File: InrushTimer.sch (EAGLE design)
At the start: 71 parts, among them IC1 TLC272D, IC2 555, IC3 4076N, Q2 TRANSISTOR-FET_2N7002, Q3 TRANSISTOR-FET_2N7002, Q4 TRANSISTOR-FET_2N7002, Q5 TRANSISTOR-FET_2N7002, Q6 DIODES_ZTX451DIODES_ZTX451_0_0, T1 MMBTA05, U1 ROHM_BY_ELEMENT14_BATCH_1_BU4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

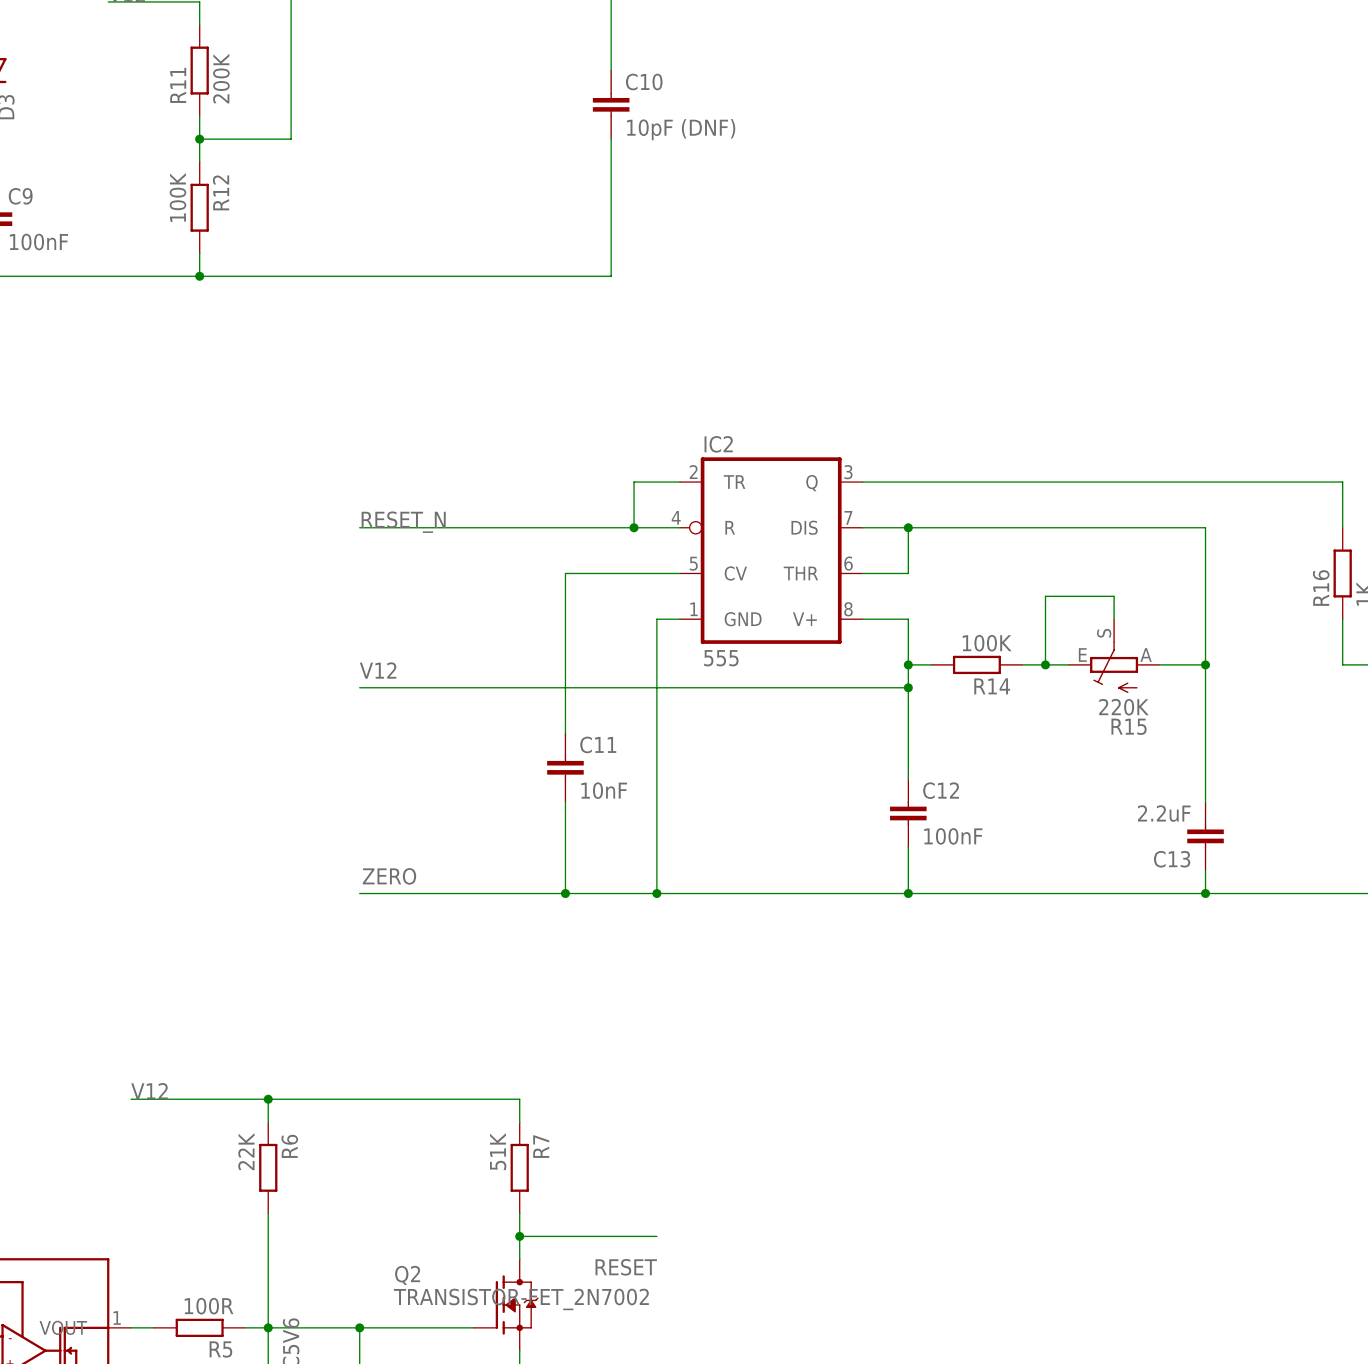
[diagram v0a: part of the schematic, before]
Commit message: Refitted the timer and pulse generator.
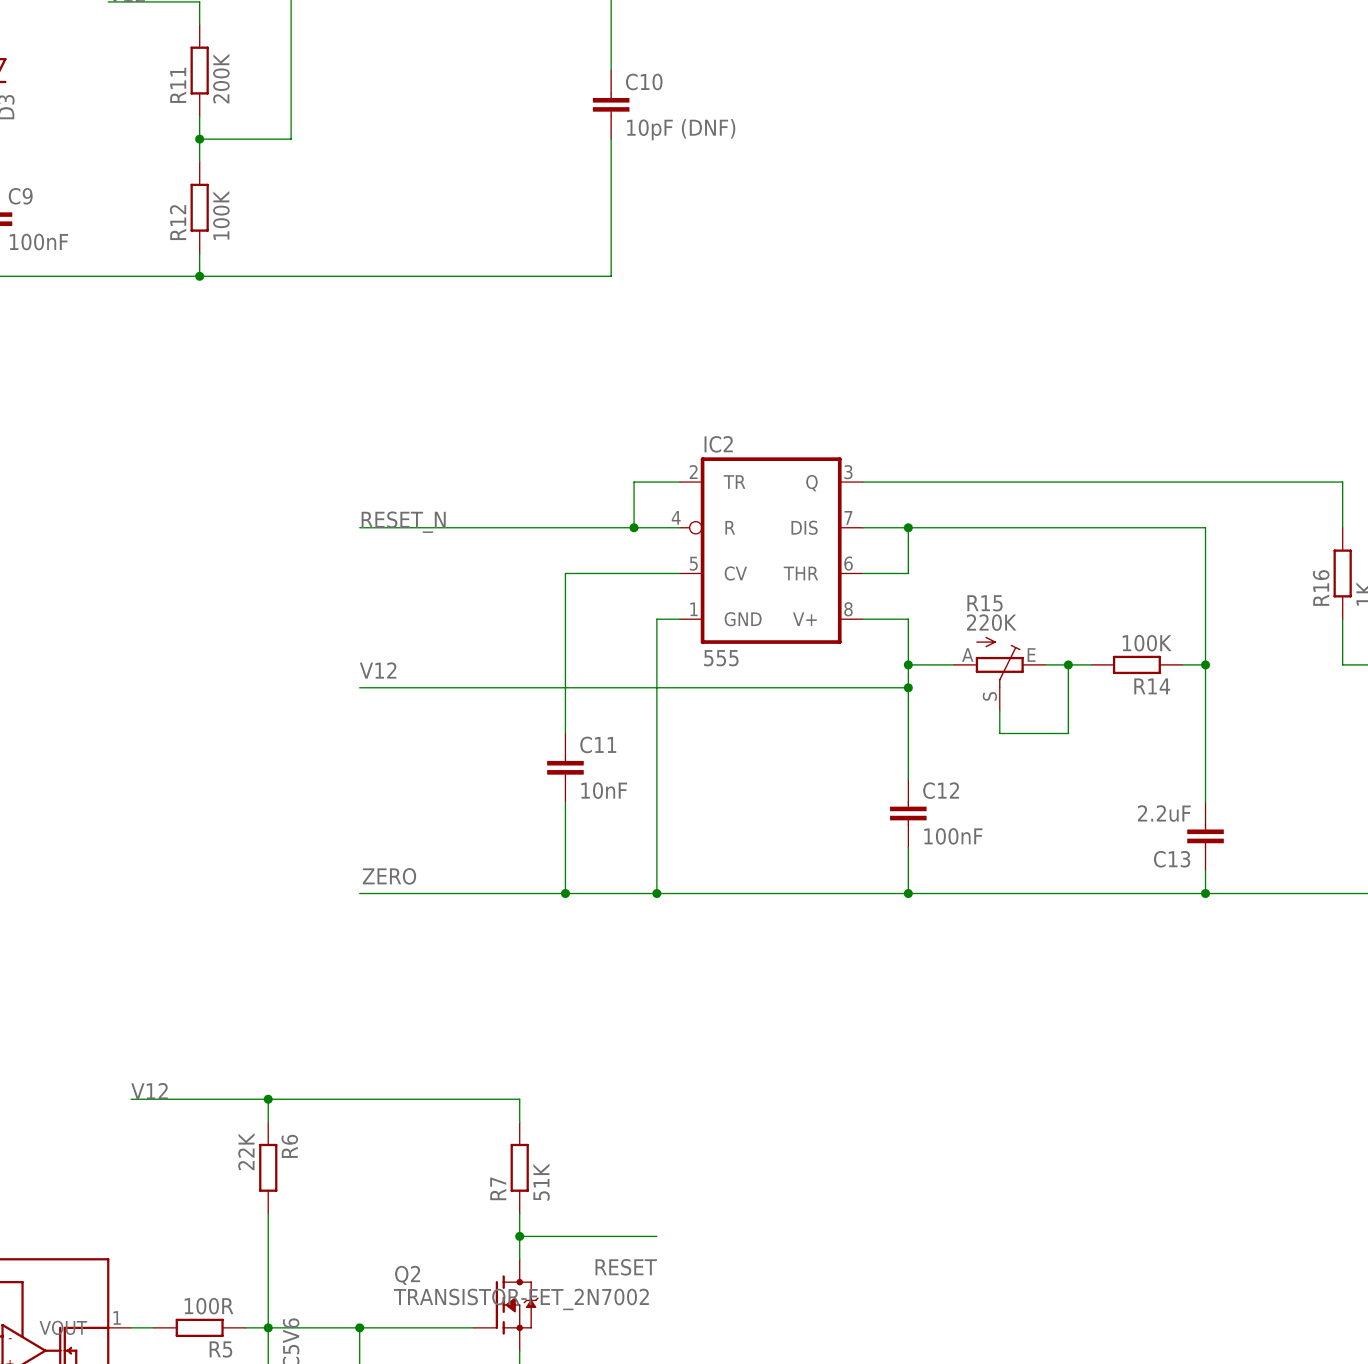
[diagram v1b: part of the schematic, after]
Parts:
- D5: device diode:DIODE-DP41-10V -> diode:DIODE-DO41-10VN
- D6: device diode:DIODE-DP41-10V -> diode:DIODE-DO41-7.6
- R15: device pot:TRIM_EU-CA6H_MOD -> pot:TRIM_EU-CA6H
- R7: device rcl:R-EU_0207/7 -> rcl:R-EU_0207/2V
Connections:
- net N$2: now also R14.2; no longer R14.1
- net N$28: now also R14.1; no longer R15.A
- net RESET: now also R7.1; no longer R7.2
- net THRESH: now also R12.2; no longer R12.1
- net V12: now also R15.A, R7.2; no longer R14.2, R7.1
- net ZERO: now also R12.1; no longer R12.2
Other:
- moved on the sheet: R12, R14, R15, R7
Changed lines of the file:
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@@
 <part name="R1" library="rcl" deviceset="R-EU_" device="0207/2V" value="4K7"/>
 <part name="R8" library="rcl" deviceset="R-EU_" device="0207/2V" value="22K"/>
-<part name="D5" library="diode" deviceset="DIODE-" device="DP41-10V" value="1n4001"/>
+<part name="D5" library="diode" deviceset="DIODE-" device="DO41-10VN" value="1n4001"/>
 <part name="R9" library="rcl" deviceset="R-EU_" device="0207/7" value="9.1M"/>
 <part name="R11" library="rcl" deviceset="R-EU_" device="0207/2V" value="200K"/>
 <part name="R12" library="rcl" deviceset="R-EU_" device="0207/2V" value="100K"/>
 <part name="IC3" library="40xx" deviceset="4076" device="N"/>
-<part name="D6" library="diode" deviceset="DIODE-" device="DP41-10V" value="1n4001"/>
+<part name="D6" library="diode" deviceset="DIODE-" device="DO41-7.6" value="1n4001"/>
 <part name="R13" library="rcl" deviceset="R-EU_" device="0207/2V" value="200K"/>
 <part name="R2" library="rcl" deviceset="R-EU_" device="0207/7" value="27K"/>
-<part name="R7" library="rcl" deviceset="R-EU_" device="0207/7" value="51K"/>
+<part name="R7" library="rcl" deviceset="R-EU_" device="0207/2V" value="51K"/>
 <part name="R6" library="rcl" deviceset="R-EU_" device="0207/2V" value="22K"/>
 <part name="R3" library="rcl" deviceset="R-EU_" device="0207/2V" value="10K"/>
@@
 <part name="R17" library="rcl" deviceset="R-EU_" device="0207/2V" value="51K"/>
 <part name="C12" library="rcl" deviceset="C-EU" device="050-024X044" value="100nF"/>
-<part name="R15" library="pot" deviceset="TRIM_EU-" device="CA6H_MOD" value="220K"/>
+<part name="R15" library="pot" deviceset="TRIM_EU-" device="CA6H" value="220K"/>
 <part name="X4" library="con-wago-500" deviceset="W237-102" device=""/>
 <part name="C11" library="rcl" deviceset="C-EU" device="050-024X044" value="10nF"/>
@@
 <instance part="R9" gate="G$1" x="-38.1" y="45.72" rot="R90"/>
 <instance part="R11" gate="G$1" x="0" y="60.96" rot="R90"/>
-<instance part="R12" gate="G$1" x="0" y="45.72" rot="R270"/>
+<instance part="R12" gate="G$1" x="0" y="45.72" rot="R90"/>
 <instance part="IC3" gate="A" x="223.52" y="-7.62"/>
 <instance part="IC3" gate="P" x="190.5" y="-20.32"/>
@@
 <instance part="R13" gate="G$1" x="22.86" y="91.44" rot="R180"/>
 <instance part="R2" gate="G$1" x="-73.66" y="-55.88" rot="R90"/>
-<instance part="R7" gate="G$1" x="35.56" y="-60.96" rot="R270"/>
+<instance part="R7" gate="G$1" x="35.56" y="-60.96" rot="R90"/>
 <instance part="R6" gate="G$1" x="7.62" y="-60.96" rot="R270"/>
 <instance part="R3" gate="G$1" x="-73.66" y="-76.2" rot="R90"/>
@@
 <instance part="C6" gate="G$1" x="-35.56" y="68.58" rot="R90"/>
 <instance part="C8" gate="G$1" x="-27.94" y="101.6"/>
-<instance part="R14" gate="G$1" x="86.36" y="-5.08" rot="R180"/>
+<instance part="R14" gate="G$1" x="104.14" y="-5.08" rot="R180"/>
 <instance part="C13" gate="G$1" x="111.76" y="-25.4" rot="R180"/>
 <instance part="R16" gate="G$1" x="127" y="5.08" rot="R90"/>
 <instance part="R17" gate="G$1" x="144.78" y="15.24" rot="R270"/>
 <instance part="C12" gate="G$1" x="78.74" y="-20.32"/>
-<instance part="R15" gate="1" x="101.6" y="-5.08" rot="R90"/>
+<instance part="R15" gate="1" x="88.9" y="-5.08" rot="R270"/>
 <instance part="X4" gate="-1" x="386.08" y="-10.16" rot="R180"/>
 <instance part="X4" gate="-2" x="386.08" y="-15.24" rot="R180"/>
@@
 <label x="-7.62" y="-53.34" size="1.778" layer="95"/>
 <wire x1="35.56" y1="-53.34" x2="7.62" y2="-53.34" width="0.1524" layer="91"/>
-<pinref part="R7" gate="G$1" pin="1"/>
 <wire x1="7.62" y1="-53.34" x2="-7.62" y2="-53.34" width="0.1524" layer="91"/>
-<wire x1="35.56" y1="-55.88" x2="35.56" y2="-53.34" width="0.1524" layer="91"/>
 <pinref part="R6" gate="G$1" pin="1"/>
 <wire x1="7.62" y1="-55.88" x2="7.62" y2="-53.34" width="0.1524" layer="91"/>
 <junction x="7.62" y="-53.34"/>
+<pinref part="R7" gate="G$1" pin="2"/>
+<wire x1="35.56" y1="-55.88" x2="35.56" y2="-53.34" width="0.1524" layer="91"/>
 </segment>
 <segment>
 <wire x1="78.74" y1="-17.78" x2="78.74" y2="-7.62" width="0.1524" layer="91"/>
 <wire x1="73.66" y1="0" x2="78.74" y2="0" width="0.1524" layer="91"/>
+<junction x="78.74" y="-7.62"/>
 <wire x1="78.74" y1="-7.62" x2="78.74" y2="-5.08" width="0.1524" layer="91"/>
-<junction x="78.74" y="-7.62"/>
 <wire x1="78.74" y1="-5.08" x2="78.74" y2="0" width="0.1524" layer="91"/>
 <wire x1="78.74" y1="-7.62" x2="17.78" y2="-7.62" width="0.1524" layer="91"/>
 <label x="17.78" y="-6.604" size="1.778" layer="95"/>
-<pinref part="R14" gate="G$1" pin="2"/>
 <pinref part="C12" gate="G$1" pin="1"/>
-<wire x1="81.28" y1="-5.08" x2="78.74" y2="-5.08" width="0.1524" layer="91"/>
+<pinref part="IC2" gate="A" pin="V+"/>
+<pinref part="R15" gate="1" pin="A"/>
+<wire x1="83.82" y1="-5.08" x2="78.74" y2="-5.08" width="0.1524" layer="91"/>
 <junction x="78.74" y="-5.08"/>
-<pinref part="IC2" gate="A" pin="V+"/>
 </segment>
 <segment>
@@
 <junction x="-66.04" y="38.1"/>
 <label x="-76.2" y="38.1" size="1.778" layer="95"/>
-<pinref part="R12" gate="G$1" pin="2"/>
-<wire x1="0" y1="40.64" x2="0" y2="38.1" width="0.1524" layer="91"/>
-<junction x="0" y="38.1"/>
 <pinref part="R8" gate="G$1" pin="1"/>
 <wire x1="-66.04" y1="50.8" x2="-66.04" y2="48.26" width="0.1524" layer="91"/>
 <junction x="-66.04" y="48.26"/>
+<pinref part="R12" gate="G$1" pin="1"/>
+<wire x1="0" y1="40.64" x2="0" y2="38.1" width="0.1524" layer="91"/>
+<junction x="0" y="38.1"/>
 </segment>
 <segment>
@@
 <wire x1="35.56" y1="-68.58" x2="50.8" y2="-68.58" width="0.1524" layer="91"/>
 <wire x1="35.56" y1="-68.58" x2="35.56" y2="-71.12" width="0.1524" layer="91"/>
-<pinref part="R7" gate="G$1" pin="2"/>
+<pinref part="Q2" gate="G$1" pin="D"/>
+<pinref part="R7" gate="G$1" pin="1"/>
 <wire x1="35.56" y1="-68.58" x2="35.56" y2="-66.04" width="0.1524" layer="91"/>
 <junction x="35.56" y="-68.58"/>
-<pinref part="Q2" gate="G$1" pin="D"/>
 </segment>
 </net>
@@
 <pinref part="IC1" gate="A" pin="-IN"/>
 <wire x1="12.7" y1="73.66" x2="10.16" y2="73.66" width="0.1524" layer="91"/>
-<pinref part="R12" gate="G$1" pin="1"/>
-<wire x1="0" y1="50.8" x2="0" y2="53.34" width="0.1524" layer="91"/>
 <wire x1="0" y1="53.34" x2="10.16" y2="53.34" width="0.1524" layer="91"/>
 <pinref part="R11" gate="G$1" pin="1"/>
 <wire x1="0" y1="55.88" x2="0" y2="53.34" width="0.1524" layer="91"/>
+<pinref part="R12" gate="G$1" pin="2"/>
+<wire x1="0" y1="50.8" x2="0" y2="53.34" width="0.1524" layer="91"/>
 <junction x="0" y="53.34"/>
 </segment>
@@
 <wire x1="78.74" y1="10.16" x2="111.76" y2="10.16" width="0.1524" layer="91"/>
 <wire x1="111.76" y1="10.16" x2="111.76" y2="-5.08" width="0.1524" layer="91"/>
-<wire x1="111.76" y1="-5.08" x2="111.76" y2="-20.32" width="0.1524" layer="91"/>
-<junction x="111.76" y="-5.08"/>
-<pinref part="R15" gate="1" pin="A"/>
-<wire x1="111.76" y1="-5.08" x2="106.68" y2="-5.08" width="0.1524" layer="91"/>
 <pinref part="IC2" gate="A" pin="THR"/>
 <pinref part="IC2" gate="A" pin="DIS"/>
+<pinref part="R14" gate="G$1" pin="1"/>
+<wire x1="111.76" y1="-5.08" x2="111.76" y2="-20.32" width="0.1524" layer="91"/>
+<wire x1="109.22" y1="-5.08" x2="111.76" y2="-5.08" width="0.1524" layer="91"/>
+<junction x="111.76" y="-5.08"/>
 </segment>
 </net>
@@
 </segment>
 </net>
-<net name="N$2" class="0">
-<segment>
-<pinref part="R15" gate="1" pin="S"/>
-<wire x1="101.6" y1="0" x2="101.6" y2="2.54" width="0.1524" layer="91"/>
-<wire x1="101.6" y1="2.54" x2="93.98" y2="2.54" width="0.1524" layer="91"/>
-<wire x1="93.98" y1="2.54" x2="93.98" y2="-5.08" width="0.1524" layer="91"/>
-<pinref part="R15" gate="1" pin="E"/>
-<wire x1="93.98" y1="-5.08" x2="96.52" y2="-5.08" width="0.1524" layer="91"/>
-<pinref part="R14" gate="G$1" pin="1"/>
-<wire x1="93.98" y1="-5.08" x2="91.44" y2="-5.08" width="0.1524" layer="91"/>
-<junction x="93.98" y="-5.08"/>
-</segment>
-</net>
 <net name="N$5" class="0">
 <segment>
@@
 </segment>
 </net>
+<net name="N$2" class="0">
+<segment>
+<pinref part="R15" gate="1" pin="E"/>
+<pinref part="R14" gate="G$1" pin="2"/>
+<wire x1="93.98" y1="-5.08" x2="96.52" y2="-5.08" width="0.1524" layer="91"/>
+<pinref part="R15" gate="1" pin="S"/>
+<wire x1="96.52" y1="-5.08" x2="99.06" y2="-5.08" width="0.1524" layer="91"/>
+<wire x1="88.9" y1="-10.16" x2="88.9" y2="-12.7" width="0.1524" layer="91"/>
+<wire x1="88.9" y1="-12.7" x2="96.52" y2="-12.7" width="0.1524" layer="91"/>
+<wire x1="96.52" y1="-12.7" x2="96.52" y2="-5.08" width="0.1524" layer="91"/>
+<junction x="96.52" y="-5.08"/>
+</segment>
+</net>

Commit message: First complete routing fit. Passes design rules.
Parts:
- D8: value 1N4148DO35-7 -> 1N4148DO35-10; device diode:1N4148DO35-7 -> diode:1N4148DO35-10
- R22, R23: device rcl:R-EU_0207/2V -> rcl:R-EU_0207/7
- R25: device rcl:R-EU_0207/7 -> rcl:R-EU_0207/2V
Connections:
- net N$15: now also R25.1; no longer R25.2
- net N$16: now also IC3A.D2; no longer IC3A.D1
- net N$17: now also R25.2; no longer R25.1
- net N$20: now also X3-1.KL; no longer X3-2.KL
- net N$21: now also X3-2.KL; no longer X3-1.KL
- net N$22: now also R19.1; no longer R20.1
- net N$30: now also R20.1; no longer R19.1
- net RESET_N: now also R6.1; no longer R6.2
- net V12: now also IC3A.D1, R6.2; no longer IC3A.D2, R6.1
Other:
- moved on the sheet: C15, C16, D10, D11, D8, D9, R22, R23, R25, R6, SJ1, X3-1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
